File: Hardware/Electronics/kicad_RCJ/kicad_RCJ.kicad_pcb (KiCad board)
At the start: 2 copper layers, 114.9 x 159.4 mm, 83 parts, among them J10 Conn_01x04_M1_extra, J11 Conn_01x04_M2_extra, J12 Conn_01x04_M3_extra, J13 Conn_01x04_M4_extra, J14 Conn_01x06_teensy_left_extra, J15 Conn_01x04_teensy_right_extra, J16 Conn_01x07_IO_expander_extra, J17 Conn_02x03_I2C, J18 Conn_02x05_3V3_GND, J19 Conn_02x05_5V_GND, J2 Conn_01x06_IMU_extra, J20 Conn_01x06_BNO085_extra, J21 Conn_01x06_ISM20948_extra, J22 Conn_01x02_LSM5DSOX_LIS3MDL_e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, J23 VBAT_meas_conn, J24 Conn_01x02, J25 Conn_01x02, J26 Conn_01x02, J27 Conn_01x02, J28 Conn_01x02_5V, J29 Conn_01x02_3.3V, J3 Conn_01x02_colsens_interrupt, J30 Conn_01x05_photoresistors, J4 Conn_01x02_5V, J5 Conn_01x02_3V3, J6 Conn_01x02_I2C1, J7 Conn_01x01_LOP, J8 Conn_01x03_IO_expander_interr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, J9 Conn_01x06_LED, M5 Servo1, M6 Servo2, U1 DRV8874, U12 VL53L0/1X, U13 VL53L0/1X, U14 VL53L0/1X, U15 VL53L0/1X, U16 VL53L0/1X, U17 VL53L0/1X, U18 VL53L0/1X, U2 DRV8874, U20 BNO085, U21 ICM20948, U22 LSM6DSOX+LIS3MDL, U23 TCS34725, U24 APDS9960, U25 VL53L0/1X, U3 DRV8874, U4 DRV8874

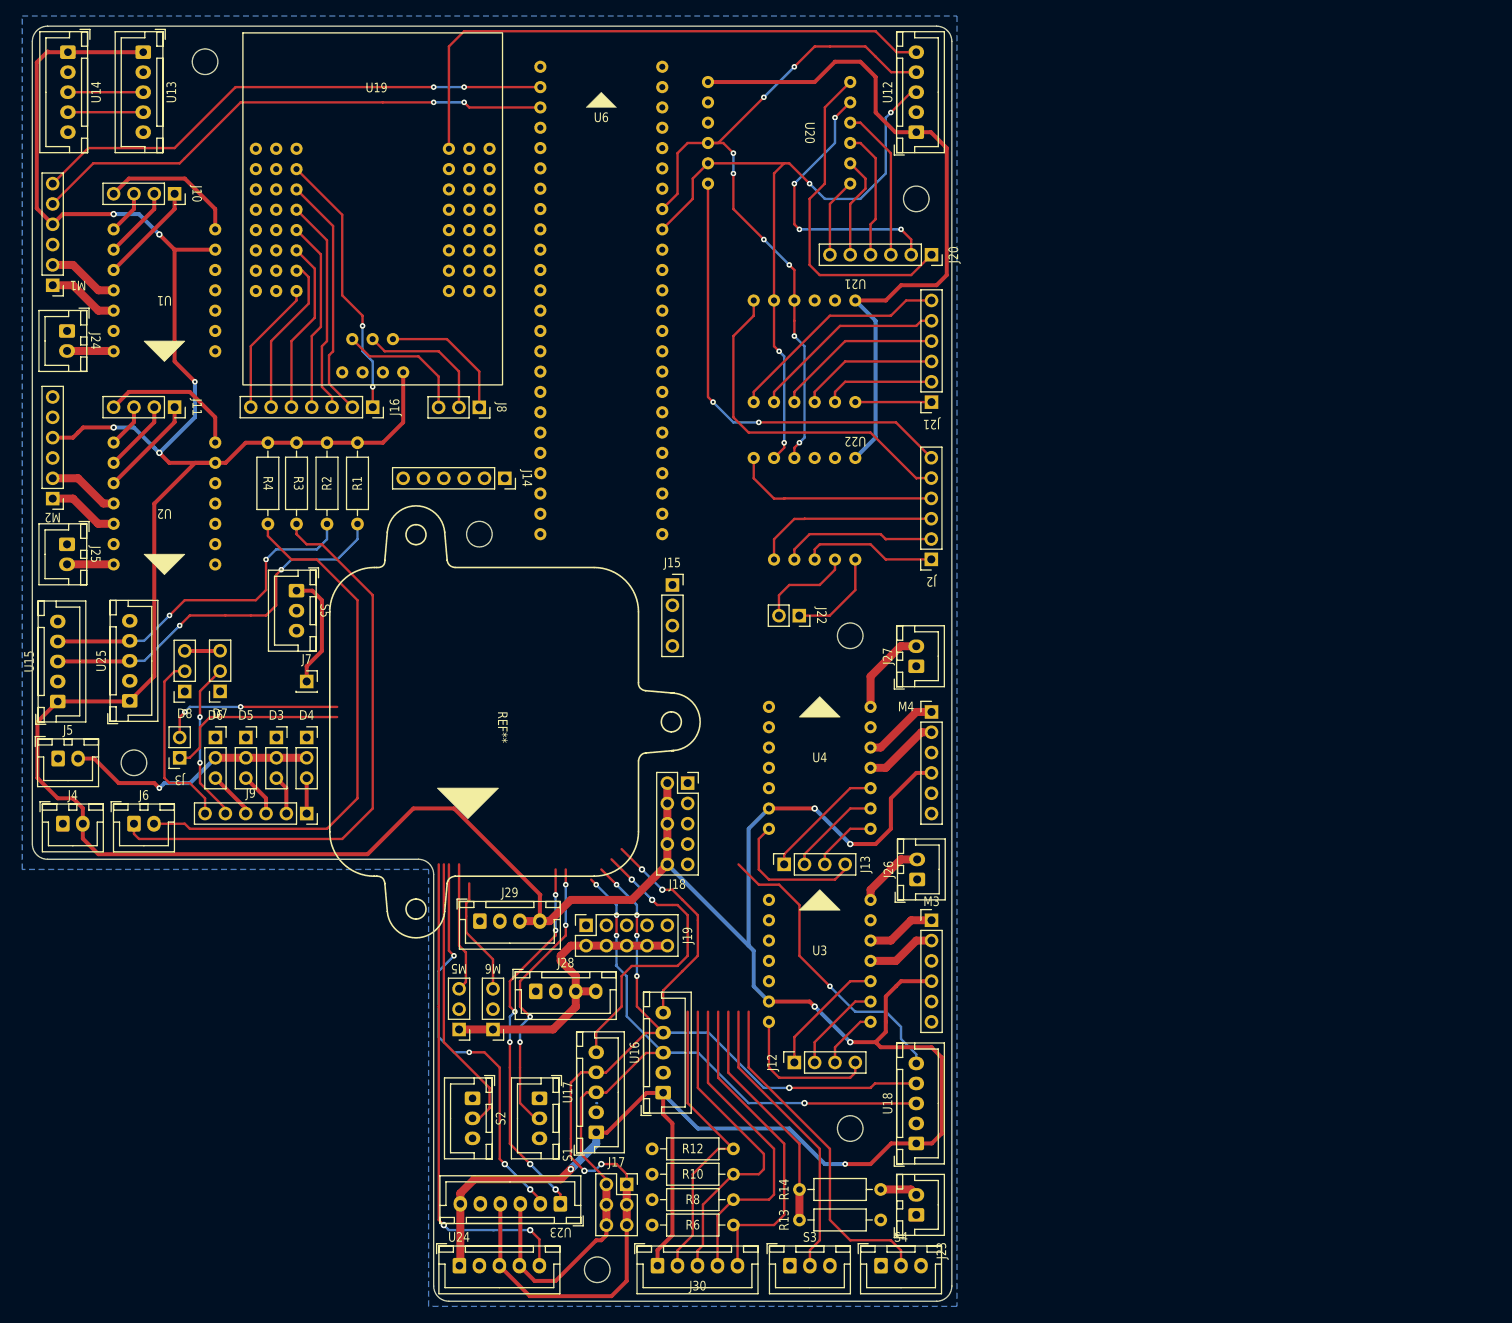
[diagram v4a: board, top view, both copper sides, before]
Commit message: continued routing of outer sections and rearranged parts of schematic for better routing
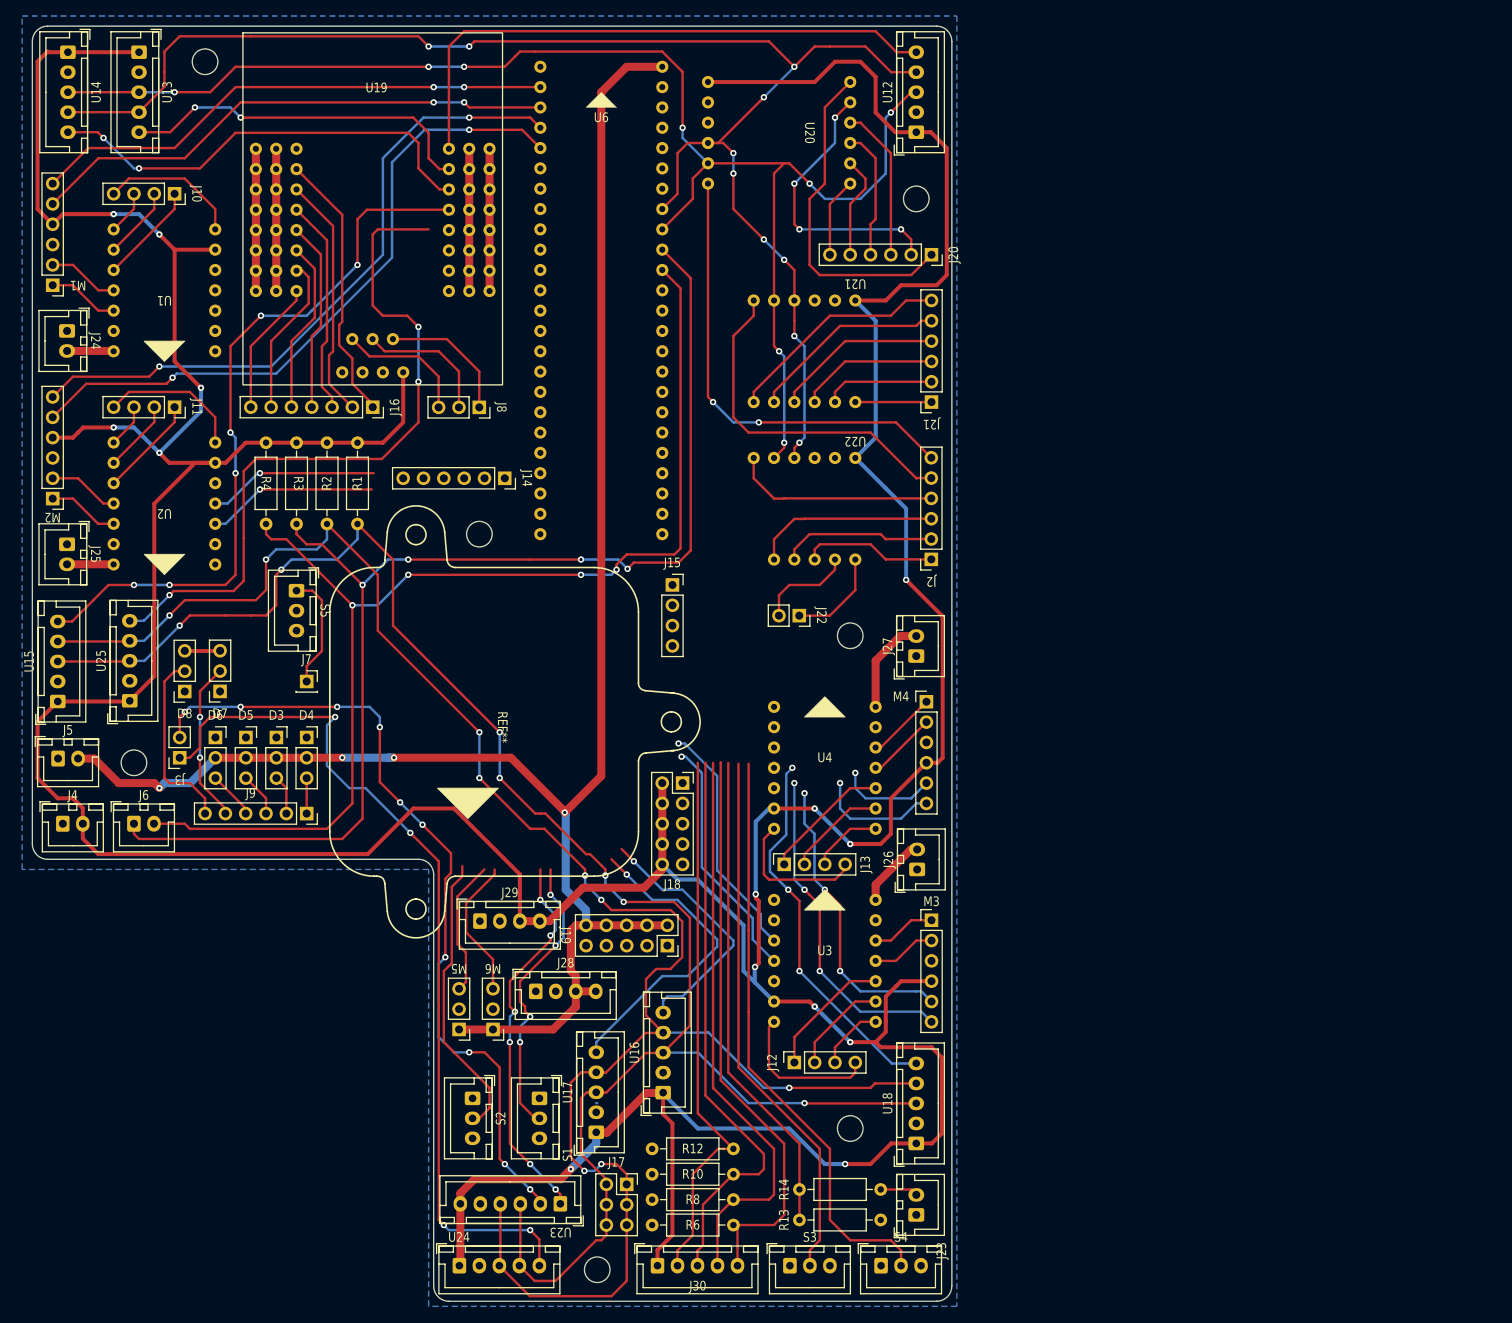
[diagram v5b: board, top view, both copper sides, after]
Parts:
- moved J19 10.5 mm to (112.4, 148.0), turned to -90 degrees
- moved M4 1.42 mm to (144.8, 117.5)
- moved J27 1.27 mm to (143.5, 111.8)
- moved J26 1.25 mm to (143.6, 138.4)
- moved J18 0.64 mm to (114.3, 127.6)
- moved U3 0.64 mm to (125.7, 157.5)
- moved U4 0.64 mm to (125.7, 133.3)
- moved U13 0.53 mm to (46.4, 36.3)
- moved R4 0.23 mm to (62.2, 85.1)
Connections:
- net Net-(J24-Pin_2) renamed /+6V_1
- net Net-(J25-Pin_2) renamed /+6V_2
- net Net-(J26-Pin_2) renamed /+6V_3
- net Net-(J27-Pin_2) renamed /+6V_4
- net Net-(U12-XSHUT) renamed /U12_XSHUT
- net Net-(U17-XSHUT) renamed /U17_XSHUT
- net Net-(U18-XSHUT) renamed /U18_XSHUT
- net Net-(U19-PB7) renamed /U25_XSHUT
- U13 pad 5: Net-(U13-XSHUT) -> /U13_XSHUT
- U14 pad 5: Net-(U14-XSHUT) -> /U14_XSHUT
- U15 pad 5: Net-(U15-XSHUT) -> /U15_XSHUT
- U16 pad 5: Net-(U16-XSHUT) -> /U16_XSHUT
- U19 pad 10: Net-(U15-XSHUT) -> /U13_XSHUT
- U19 pad 11: Net-(U13-XSHUT) -> /U14_XSHUT
- U19 pad 12: Net-(U16-XSHUT) -> /U15_XSHUT
- U19 pad 13: Net-(U14-XSHUT) -> /U16_XSHUT
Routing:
- net SCL: track 272.6 -> 430.1 mm, vias 17 -> 19
- net +5V: track 75.4 -> 228.6 mm, vias 1 -> 4
- net SDA: track 256.2 -> 403.5 mm, vias 10 -> 15
- net /U15_XSHUT: track 0.00 -> 91.2 mm, vias 0 -> 6
- net /U25_XSHUT: track 0.00 -> 89.3 mm, vias 0 -> 3
- net Net-(M2-ENC_A_OUT): track 0.00 -> 83.8 mm, vias 0 -> 2
- net Net-(M2-ENC_B_OUTPUT): track 0.00 -> 83.0 mm, vias 0 -> 2
- net SDA1: track 73.6 -> 155.4 mm, vias 0 -> 4
- net SCL1: track 68.1 -> 147.0 mm, vias 0 -> 4
- net /U14_XSHUT: track 0.00 -> 56.1 mm, vias 0 -> 2
- net +3.3V: track 613.6 -> 662.8 mm, vias 11 -> 14
- net /U13_XSHUT: track 0.00 -> 45.1 mm, vias 0 -> 2
- net Net-(M3-ENC_B_OUTPUT): track 0.00 -> 41.4 mm, vias 0 -> 3
- net Net-(M3-ENC_A_OUT): track 0.00 -> 37.1 mm, vias 0 -> 3
- net unconnected-(U19-VCC-Pad25): track 0.00 -> 35.6 mm
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
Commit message: finished essential routing (some extras left)
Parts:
- U19: footprint RCJ2024_kicad_footprints:IO_Expander -> RCJ2024_kicad_footprints:IO_Expander_nopower
- moved J14 9.53 mm to (92.2, 99.1), turned to 180 degrees
- moved REF** 6.84 mm to (85.3, 90.7)
- moved J15 1.27 mm to (112.3, 103.9)
- moved J8 1.26 mm to (87.6, 80.6)
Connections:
- net Net-(J30-Pin_2) renamed /PR4
- net Net-(J30-Pin_3) renamed /PR3
- net Net-(J30-Pin_4) renamed /PR2
- net Net-(J30-Pin_5) renamed /PR1
- net Net-(M1-ENC_A_OUT) renamed /M1_ENCA
- net Net-(M1-ENC_B_OUTPUT) renamed /M1_ENCB
- net Net-(M2-ENC_A_OUT) renamed /M2_ENCA
- net Net-(M2-ENC_B_OUTPUT) renamed /M2_ENCB
- net Net-(S3-NO) renamed /BMP3
- net Net-(S4-NO) renamed /BMP4
- net Net-(U6-20/A6/TX5) renamed /VBAT_MEAS
- J14 pad 1: Net-(J14-Pin_1) -> unconnected-(J14-Pin_1-Pad1)
- J14 pad 2: Net-(J14-Pin_2) -> unconnected-(J14-Pin_2-Pad2)
- J14 pad 3: Net-(J14-Pin_3) -> unconnected-(J14-Pin_3-Pad3)
- J14 pad 4: Net-(J14-Pin_4) -> unconnected-(J14-Pin_4-Pad4)
- J14 pad 5: Net-(J14-Pin_5) -> unconnected-(J14-Pin_5-Pad5)
- J14 pad 6: Net-(J14-Pin_6) -> unconnected-(J14-Pin_6-Pad6)
- J15 pad 1: Net-(J15-Pin_1) -> unconnected-(J15-Pin_1-Pad1)
- J15 pad 2: Net-(J15-Pin_2) -> unconnected-(J15-Pin_2-Pad2)
- J15 pad 3: Net-(J15-Pin_3) -> unconnected-(J15-Pin_3-Pad3)
- J15 pad 4: Net-(J15-Pin_4) -> unconnected-(J15-Pin_4-Pad4)
- M3 pad 5: Net-(M3-ENC_A_OUT) -> /M3_ENCA
- M3 pad 6: Net-(M3-ENC_B_OUTPUT) -> /M3_ENCB
- M4 pad 5: Net-(M4-ENC_A_OUT) -> /M4_ENCA
- M4 pad 6: Net-(M4-ENC_B_OUTPUT) -> /M4_ENCB
- M5 pad 3: Net-(M5-SIGNAL) -> /M5_SIG
- M6 pad 3: Net-(M6-SIGNAL) -> /M6_SIG
- S1 pad 2: Net-(S1-NO) -> /BMP1
- S2 pad 2: Net-(S2-NO) -> /BMP2
- U1 pad 3: Net-(U1-EN/IN1) -> /M1_IN1
- U1 pad 4: Net-(U1-PH/IN2) -> /M1_IN2
- U19 pad 11: /U14_XSHUT -> /U15_XSHUT
- U19 pad 12: /U15_XSHUT -> /U25_XSHUT
- U19 pad 16: /U25_XSHUT -> /TCS34725_LED
- U19 pad 8: Net-(U19-PA7) -> /U14_XSHUT
- U2 pad 3: Net-(U2-EN/IN1) -> /M2_IN1
- U2 pad 4: Net-(U2-PH/IN2) -> /M2_IN2
- U23 pad 1: Net-(U19-PA7) -> /TCS34725_LED
- U3 pad 3: Net-(U3-EN/IN1) -> /M3_IN1
- U3 pad 4: Net-(U3-PH/IN2) -> /M3_IN2
- U4 pad 3: Net-(U4-EN/IN1) -> /M4_IN1
- U4 pad 4: Net-(U4-PH/IN2) -> /M4_IN2
- U6 pad 10: Net-(U3-EN/IN1) -> unconnected-(U6-10/CS-Pad10)
- U6 pad 11: Net-(U4-EN/IN1) -> unconnected-(U6-11/MOSI-Pad11)
- U6 pad 12: Net-(J14-Pin_6) -> unconnected-(U6-12/MISO-Pad12)
- U6 pad 21: Net-(J15-Pin_1) -> unconnected-(U6-21/A7/RX5-Pad21)
- U6 pad 22: Net-(M6-SIGNAL) -> /M4_ENCB
- U6 pad 23: Net-(M5-SIGNAL) -> /M4_ENCA
- U6 pad 24: Net-(U1-PH/IN2) -> /M5_SIG
- U6 pad 25: Net-(U2-PH/IN2) -> /M6_SIG
- U6 pad 26: Net-(J14-Pin_5) -> unconnected-(U6-26/A12/MOSI1-Pad26)
- U6 pad 27: Net-(J14-Pin_4) -> unconnected-(U6-27/A13/SCK1-Pad27)
- U6 pad 28: Net-(U3-PH/IN2) -> /M3_IN1
- U6 pad 29: Net-(U4-PH/IN2) -> /M3_IN2
- U6 pad 30: Net-(J14-Pin_3) -> unconnected-(U6-Pad30)
- U6 pad 31: Net-(J14-Pin_2) -> /BMP2
- U6 pad 32: Net-(J14-Pin_1) -> /BMP1
- U6 pad 35: Net-(S2-NO) -> unconnected-(U6-35/TX8-Pad35)
- U6 pad 36: Net-(S1-NO) -> /M4_IN2
- U6 pad 37: Net-(J15-Pin_4) -> /M4_IN1
- U6 pad 38: Net-(J15-Pin_3) -> /M3_ENCB
- U6 pad 39: Net-(J15-Pin_2) -> /M3_ENCA
- U6 pad 4: Net-(M3-ENC_B_OUTPUT) -> /M1_IN2
- U6 pad 44: GND -> unconnected-(U6-GND-Pad44)
- U6 pad 46: GND -> unconnected-(U6-GND-Pad46)
- U6 pad 5: Net-(M3-ENC_A_OUT) -> /M1_IN1
- U6 pad 6: Net-(M4-ENC_B_OUTPUT) -> /M2_IN2
- U6 pad 7: Net-(M4-ENC_A_OUT) -> /M2_IN1
- U6 pad 8: Net-(U1-EN/IN1) -> unconnected-(U6-8/TX2-Pad8)
- U6 pad 9: Net-(U2-EN/IN1) -> unconnected-(U6-Pad9)
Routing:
- net /TCS34725_LED: track 0.00 -> 131.4 mm, vias 0 -> 10
- net /M4_ENCB: track 0.00 -> 106.7 mm, vias 0 -> 2
- net /M4_ENCA: track 0.00 -> 106.5 mm, vias 0 -> 2
- net /U18_XSHUT: track 47.5 -> 153.0 mm, vias 3 -> 7
- net /M3_ENCB: track 0.00 -> 98.4 mm, vias 0 -> 3
- net /M3_ENCA: track 0.00 -> 98.4 mm, vias 0 -> 3
- net /U16_XSHUT: track 32.5 -> 125.4 mm, vias 1 -> 5
- net /BMP2: track 0.00 -> 90.9 mm, vias 0 -> 3
- net /U17_XSHUT: track 39.6 -> 130.1 mm, vias 1 -> 5
- net /M6_SIG: track 0.00 -> 85.9 mm, vias 0 -> 6
- net /VBAT_MEAS: track 60.8 -> 145.8 mm, vias 0 -> 2
- net /M5_SIG: track 0.00 -> 84.4 mm, vias 0 -> 4
- net /M3_IN1: track 0.00 -> 81.2 mm, vias 0 -> 5
- net /BMP1: track 0.00 -> 80.4 mm, vias 0 -> 5
- net /M3_IN2: track 0.00 -> 80.2 mm, vias 0 -> 5
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
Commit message: PCB finished?
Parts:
- added G***: LOGO, LOGO, F.Cu at (88.4, 114.1)
- H1, H2, H3, H4, H5, H6, H7: renamed from REF**; value MountingHole_3.2mm_M3 -> MountingHole
- J15: value Conn_01x04_teensy_right_extra -> Conn_01x03; footprint Connector_PinSocket_2.54mm:PinSocket_1x04_P2.54mm_Vertical -> Connector_PinSocket_2.54mm:PinSocket_1x03_P2.54mm_Vertical
- moved J14 48.9 mm to (101.6, 51.0)
- moved J15 23.2 mm to (92.0, 92.7), turned to 180 degrees
- moved H7 2.40 mm to (83.5, 92.2)
- moved H2 0.21 mm to (143.7, 54.6)
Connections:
- J14 pad 1: unconnected-(J14-Pin_1-Pad1) -> Net-(J14-Pin_1)
- J14 pad 2: unconnected-(J14-Pin_2-Pad2) -> Net-(J14-Pin_2)
- J14 pad 3: unconnected-(J14-Pin_3-Pad3) -> Net-(J14-Pin_3)
- J14 pad 4: unconnected-(J14-Pin_4-Pad4) -> Net-(J14-Pin_4)
- J14 pad 5: unconnected-(J14-Pin_5-Pad5) -> Net-(J14-Pin_5)
- J14 pad 6: unconnected-(J14-Pin_6-Pad6) -> /21_extra
- J15 pad 1: unconnected-(J15-Pin_1-Pad1) -> Net-(J15-Pin_1)
- J15 pad 2: unconnected-(J15-Pin_2-Pad2) -> Net-(J15-Pin_2)
- J15 pad 3: unconnected-(J15-Pin_3-Pad3) -> Net-(J15-Pin_3)
- U6 pad 10: unconnected-(U6-10/CS-Pad10) -> Net-(J14-Pin_3)
- U6 pad 11: unconnected-(U6-11/MOSI-Pad11) -> Net-(J14-Pin_2)
- U6 pad 12: unconnected-(U6-12/MISO-Pad12) -> Net-(J14-Pin_1)
- U6 pad 21: unconnected-(U6-21/A7/RX5-Pad21) -> /21_extra
- U6 pad 26: unconnected-(U6-26/A12/MOSI1-Pad26) -> Net-(J15-Pin_3)
- U6 pad 27: unconnected-(U6-27/A13/SCK1-Pad27) -> Net-(J15-Pin_2)
- U6 pad 30: unconnected-(U6-Pad30) -> Net-(J15-Pin_1)
- U6 pad 8: unconnected-(U6-8/TX2-Pad8) -> Net-(J14-Pin_5)
- U6 pad 9: unconnected-(U6-Pad9) -> Net-(J14-Pin_4)
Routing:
- net Net-(J14-Pin_2): track 0.00 -> 23.9 mm
- net Net-(J14-Pin_1): track 0.00 -> 23.7 mm
- net Net-(J14-Pin_4): track 0.00 -> 23.5 mm
- net Net-(J14-Pin_3): track 0.00 -> 23.5 mm
- net Net-(J14-Pin_5): track 0.00 -> 22.2 mm
- net /21_extra: track 0.00 -> 18.3 mm, vias 0 -> 1
- net Net-(J15-Pin_3): track 0.00 -> 8.20 mm
- net Net-(J15-Pin_2): track 0.00 -> 8.20 mm
- net Net-(J15-Pin_1): track 0.00 -> 5.04 mm
- net SDA: track 472.9 -> 474.9 mm
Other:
- board text added: "3V3"
- board text added: "5V"
- board text added: "I2C"
- board text added: "I2C1"
- board text added: "LOP"
- board text added: "v0.1 2023-12 ED Robotics <name?>"
- board text added: "{dblquote}PCB:n kommer vara färdig på söndag...{dblquote}"

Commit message: PCB finished and manufacturing files produced
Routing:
- net SCL: track 506.6 -> 506.1 mm, vias 22 -> 21
- net SDA: vias 17 -> 16
- net Net-(J20-Pin_2): vias 4 -> 3
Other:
- board size 114.9 x 159.4 mm -> 115.8 x 160.2 mm
- board text added: "v0.1 2023-12 ED Robotics Leopold Grinnemo"
- board text removed: "v0.1 2023-12 ED Robotics <name?>"
